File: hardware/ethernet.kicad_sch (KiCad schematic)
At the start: 6 parts, among them U1 TPD4EUSB30, U2 TPD4EUSB30, U3 MagJack-A70-112-331N126

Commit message: Lay out the 4-layer PCB
Route the board on JLCPCB's JLC04161H-7628 stackup (4 layers, 1.6 mm,
ENIG). It fits a 74 mm tube centred on its axis; the tightest part is the
USB-C port J8, 1.8 mm from the wall. DRC gives 0 errors, 0 unconnected
items and a clean schematic parity check. 21 advisory warnings remain on
the 3 mm PoE isolation guide; the README lists them.

Layout:
- the PoE primary side keeps 2.0 mm from everything else on every layer,
  enforced by manafish.kicad_dru, with a primary-only island under U5's
  input half and inner-layer voids next to primary copper
- 100 ohm (Ethernet, CSI) and 90 ohm (USB) pair classes over a solid In1
  ground; GND pours on all layers with stitching vias
- RP2354A core regulator laid out per the RP2350 datasheet, including the
  In1 cut-out under VREG_LX
- fabrication, assembly and isolation-test notes on User.Comments

Schematic and BOM:
- U3 is now the YAGEO JXF0-1012NL 4-pair PoE MagJack, with a new YAGEO
  library and STEP model drawn from datasheet J520
- C21/C24 are 4.7 nF 2 kV KEMET C1812X472KGRACTU (1812)
- U6/U7 are LTV-817S-TA1 (SMD)
- J8's four VBUS pins are joined by a local VBUS label

Libraries:
- Silvertel Ag59800: keep-out on the module-facing layer and the inner
  layer next to it; pads 1-3, 8 and 9 solder-mask defined
- LTC4162 QFN: the exposed-pad paste windows clear the thermal vias
- ABM8-272-T3 courtyard trimmed; 3D model paths fixed for ABM8, SHT45 and
  BMI270

README: new PCB section (stackup, impedance, isolation, assembly,
testing) and the power and Ethernet descriptions brought up to date.
NOTICE: the YAGEO files and the library changes.

Co-Authored-By: Claude Opus 5.5 <noreply@anthropic.com>
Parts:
- U3: value MagJack-A70-112-331N126 -> JXF0-1012NL; footprint CM5IO:TRJG0926HENL -> YAGEO:YAGEO_JXF0-1012NL; symbol CM5IO:MagJack-A70-112-331N126 -> YAGEO:JXF0-1012NL; MPN A70-112-331N126 -> JXF0-1012NL; Manufacturer EDAC -> YAGEO (Pulse); Mouser https://www.mouser.com/ProductDetail/587-A70-112-331N126 -> https://www.mouser.com/ProductDetail/673-JXF0-1012NL; Mouser PN 587-A70-112-331N126 -> 673-JXF0-1012NL
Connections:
- net +3.3V: now also U3.11 (LEDG_A), U3.13 (LEDY_A); no longer U3.15 (LEDY_A), U3.17 (LEDG_A)
- net TRD1_N: now also U3.4 (MD2-); no longer U3.6 (TRD1-)
- net VC1: now also U3.15 (VDC1+); no longer U3.11 (VC1)
- net VC2: now also U3.17 (VDC2+); no longer U3.12 (VC2)
- net VC3: now also U3.18 (VDC2-); no longer U3.13 (VC3)
- net VC4: now also U3.16 (VDC1-); no longer U3.14 (VC4)
- net at R2.1: now also U3.14 (LEDY_K); no longer U3.16 (LEDY_K)
- net at R3.1: now also U3.12 (LEDG_K); no longer U3.18 (LEDG_K)
- net at C1.1, U3.5 (MDCT): now also U3.6 (MDCT); no longer U3.4 (CT)
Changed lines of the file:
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@@
 	)
 	(symbol
-		(lib_id "CM5IO:MagJack-A70-112-331N126")
+		(lib_id "YAGEO:JXF0-1012NL")
 		(at 80.01 106.68 0)
 		(unit 1)
@@
 			)
 		)
-		(property "Value" "MagJack-A70-112-331N126"
+		(property "Value" "JXF0-1012NL"
 			(at 62.23 106.68 0)
 			(show_name no)
@@
 			)
 		)
-		(property "Footprint" "CM5IO:TRJG0926HENL"
+		(property "Footprint" "YAGEO:YAGEO_JXF0-1012NL"
 			(at 80.01 106.68 0)
 			(hide yes)
@@
 			)
 		)
-		(property "Datasheet" "https://www.mouser.com/catalog/specsheets/EDAC_A70-112-331N126.pdf"
+		(property "Datasheet" "https://www.yageogroup.com/content/datasheet/asset/file/DATASHEET_J520"
 			(at 80.01 106.68 0)
 			(hide yes)
@@
 			)
 		)
-		(property "Description" "RJ45 MagJack 1000BASE-T, PoE-capable centre taps, LEDs"
+		(property "Description" "RJ45 MagJack 1000BASE-T, 90 W 4-pair PoE (900 mA per center tap), bi-colour LEDs, THR"
 			(at 80.01 106.68 0)
 			(hide yes)
@@
 			)
 		)
-		(property "Manufacturer" "EDAC"
+		(property "Manufacturer" "YAGEO (Pulse)"
 			(at 80.01 106.68 0)
 			(hide yes)
@@
 			)
 		)
-		(property "MPN" "A70-112-331N126"
+		(property "MPN" "JXF0-1012NL"
 			(at 80.01 106.68 0)
 			(hide yes)
@@
 			)
 		)
-		(property "Mouser PN" "587-A70-112-331N126"
+		(property "Mouser PN" "673-JXF0-1012NL"
 			(at 80.01 106.68 0)
 			(hide yes)
@@
 			)
 		)
-		(property "Mouser" "https://www.mouser.com/ProductDetail/587-A70-112-331N126"
+		(property "Mouser" "https://www.mouser.com/ProductDetail/673-JXF0-1012NL"
 			(at 80.01 106.68 0)
 			(hide yes)

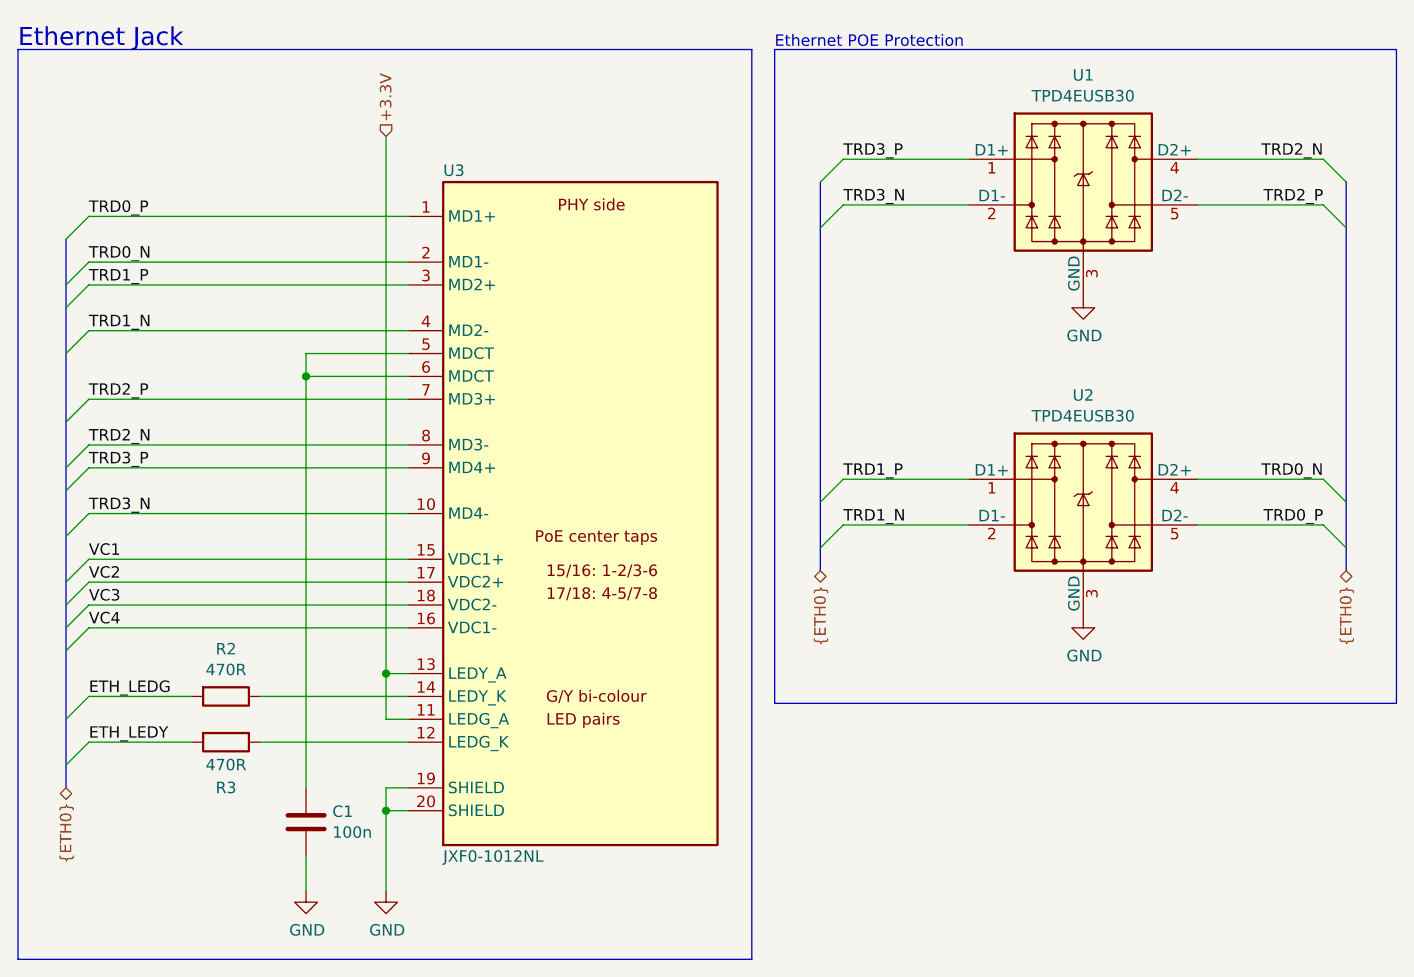
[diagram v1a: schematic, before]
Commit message: Add second camera, magnet load switch and schematic fixes
- Second camera J11 on MIPI1: I2C on ID_SD/ID_SC with 2.2k pull-ups,
  power enable on GPIO14/15 (CAM1_GPIO0/1); both cameras take 3.3 V
  from CM5_3.3V
- Magnet power switch: IC9 output is now +5V_AON, TPS22965 load switch
  IC15 drives +5V, J12 carries +5V_AON / MAG_ON / GND with R29
  pull-down; new TPS22965 symbol library
- Power: 4 A TPSM53604, 8 mOhm input sense resistor, C39/C40 bulk caps,
  F1-F3 battery polyfuses; 5 V raised to 5.115 V (R24 2.43k, 0.5 %
  feedback resistors); 47 uF at the CM5 5 V pins
- BMI270 on SPI and WSEN-PADS on I2C in serial_peripherals.kicad_sch
- Breakout headers J9/J13 with 5 V, 3.3 V and GND
- References renamed U -> IC; net classes for DPHY1, +5V, +5V_AON, +3.3V
- ERC clean (0 errors, 0 warnings); PCB update from the schematic is
  still in progress

Co-Authored-By: Claude Opus 5.5 <noreply@anthropic.com>
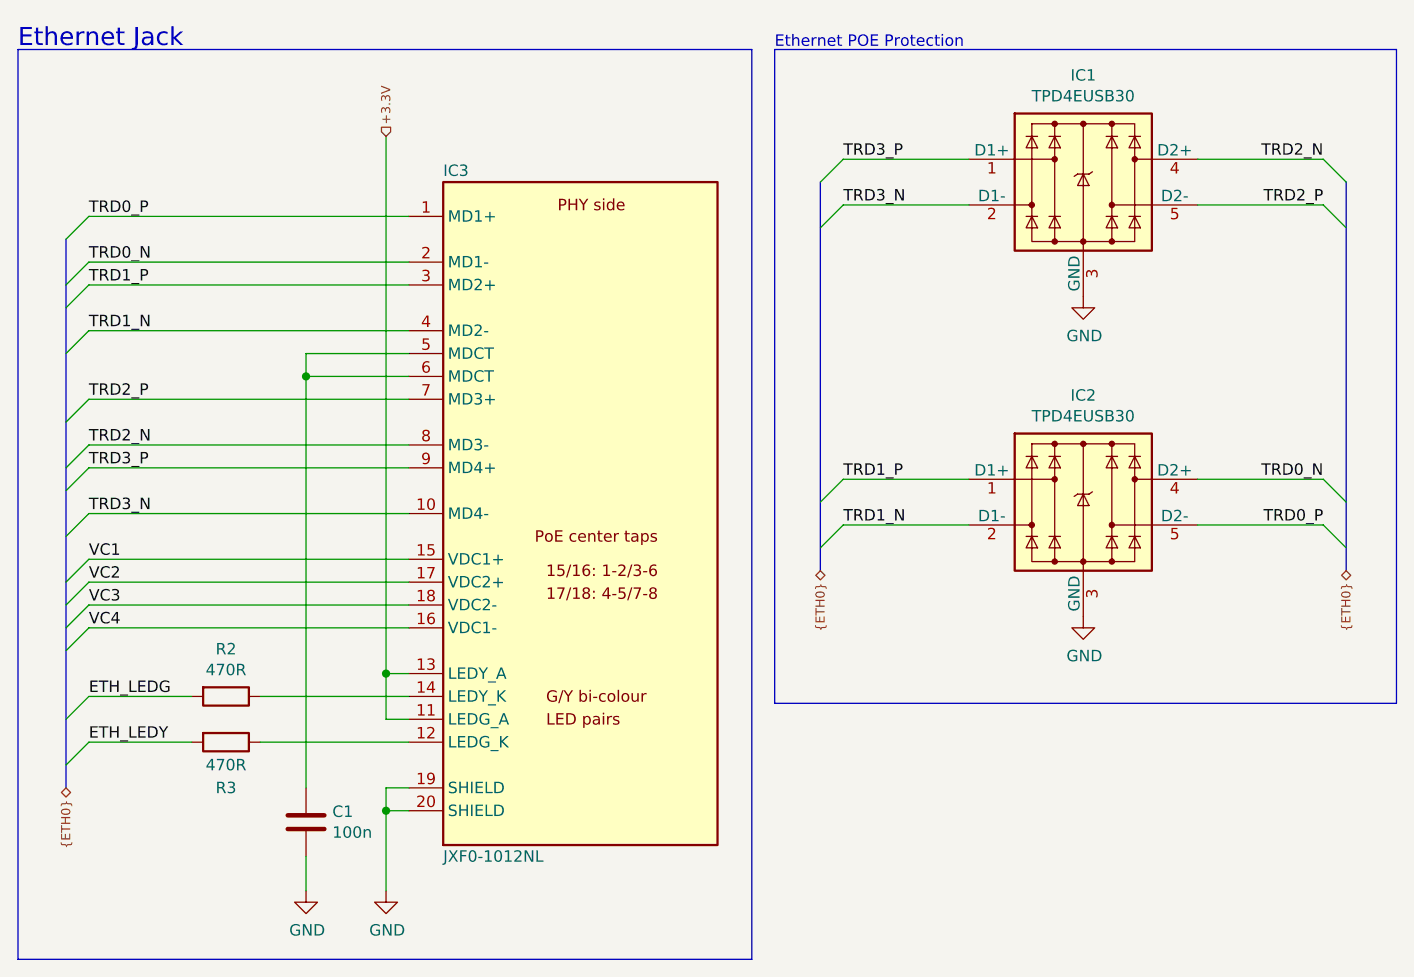
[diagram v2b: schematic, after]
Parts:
- renumbered U1 to IC1, U2 to IC2, U3 to IC3
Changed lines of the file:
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@@
 		(effects
 			(font
-				(size 1.27 1.27)
+				(size 1.016 1.016)
 			)
 			(justify right)
@@
 		(effects
 			(font
-				(size 1.27 1.27)
+				(size 1.016 1.016)
 			)
 			(justify left)
@@
 		(effects
 			(font
-				(size 1.27 1.27)
+				(size 1.016 1.016)
 			)
 			(justify right)
@@
 		(effects
 			(font
-				(size 1.27 1.27)
+				(size 1.016 1.016)
 			)
 			(justify right)
@@
 		(in_pos_files yes)
 		(dnp no)
-		(property "Reference" "U3"
+		(property "Reference" "IC3"
 			(at 62.23 30.48 0)
 			(show_name no)
@@
 			(project "manafish"
 				(path "/37283e3e-a087-4659-9b29-171eab26a1f6/ba09456f-d29b-4907-909f-45263bd46633"
-					(reference "U3")
+					(reference "IC3")
 					(unit 1)
 				)
@@
 		(in_pos_files yes)
 		(dnp no)
-		(property "Reference" "U1"
+		(property "Reference" "IC1"
 			(at 133.35 19.8882 0)
 			(show_name no)
@@
 			(project "manafish"
 				(path "/37283e3e-a087-4659-9b29-171eab26a1f6/ba09456f-d29b-4907-909f-45263bd46633"
-					(reference "U1")
+					(reference "IC1")
 					(unit 1)
 				)
@@
 		(in_pos_files yes)
 		(dnp no)
-		(property "Reference" "U2"
+		(property "Reference" "IC2"
 			(at 133.35 55.4482 0)
 			(show_name no)
@@
 			(project "manafish"
 				(path "/37283e3e-a087-4659-9b29-171eab26a1f6/ba09456f-d29b-4907-909f-45263bd46633"
-					(reference "U2")
+					(reference "IC2")
 					(unit 1)
 				)

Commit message: Add LCSC part numbers and links, fix J7 part number
- Every part found on LCSC gets an "LCSC PN" (C-number) and an "LCSC" product
  link field, in the schematic and on the PCB footprints. Exact matches where
  LCSC lists the part; equivalents with the same specs where it does not or
  has no stock (C46, C26/C28/C30/C33/C34/C40, C29, C31, R6/R7, R21, R24,
  J3/J4, J7/J9/J13). Left empty: IC3, IC5 (not on LCSC), IC10, IC12
  (JLCPCB-only listings).
- J7: the MPN 61301421121 is a 2.54 mm header, but the footprint is 1.27 mm.
  Now Wurth 62201421121 (WR-PHD 1.27 mm 2x7) with matching description,
  datasheet and Mouser fields.
- Interactive HTML BOM in hardware/bom; KiCad project file re-saved.

Co-Authored-By: Claude Opus 5.5 <noreply@anthropic.com>
Claude-Session: https://claude.ai/code/session_01AhLYztcZikG9g81njGtEr1
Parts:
- C1: LCSC (none) -> https://www.lcsc.com/product-detail/C71629.html; LCSC PN (none) -> C71629
- IC1, IC2: LCSC (none) -> https://www.lcsc.com/product-detail/C90627.html; LCSC PN (none) -> C90627
- R2, R3: LCSC (none) -> https://www.lcsc.com/product-detail/C114877.html; LCSC PN (none) -> C114877
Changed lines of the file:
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@@
+			)
+		)
+		(property "LCSC PN" "C114877"
+			(at 38.1 93.98 0)
+			(hide yes)
+			(show_name no)
+			(do_not_autoplace no)
+			(effects
+				(font
+					(size 1.27 1.27)
+				)
+			)
+		)
+		(property "LCSC" "https://www.lcsc.com/product-detail/C114877.html"
+			(at 38.1 93.98 0)
+			(hide yes)
+			(show_name no)
+			(do_not_autoplace no)
+			(effects
+				(font
+					(size 1.27 1.27)
+				)
 			)
 		)
@@
 			)
 		)
+		(property "LCSC PN" "C114877"
+			(at 38.1 88.9 0)
+			(hide yes)
+			(show_name no)
+			(do_not_autoplace no)
+			(effects
+				(font
+					(size 1.27 1.27)
+				)
+			)
+		)
+		(property "LCSC" "https://www.lcsc.com/product-detail/C114877.html"
+			(at 38.1 88.9 0)
+			(hide yes)
+			(show_name no)
+			(do_not_autoplace no)
+			(effects
+				(font
+					(size 1.27 1.27)
+				)
+			)
+		)
 		(pin "1"
 		)
@@
 			)
 		)
+		(property "LCSC PN" "C90627"
+			(at 133.35 31.75 0)
+			(hide yes)
+			(show_name no)
+			(do_not_autoplace no)
+			(effects
+				(font
+					(size 1.27 1.27)
+				)
+			)
+		)
+		(property "LCSC" "https://www.lcsc.com/product-detail/C90627.html"
+			(at 133.35 31.75 0)
+			(hide yes)
+			(show_name no)
+			(do_not_autoplace no)
+			(effects
+				(font
+					(size 1.27 1.27)
+				)
+			)
+		)
 		(pin "1"
 		)
@@
 			)
 		)
+		(property "LCSC PN" "C71629"
+			(at 46.99 102.87 0)
+			(hide yes)
+			(show_name no)
+			(do_not_autoplace no)
+			(effects
+				(font
+					(size 1.27 1.27)
+				)
+			)
+		)
+		(property "LCSC" "https://www.lcsc.com/product-detail/C71629.html"
+			(at 46.99 102.87 0)
+			(hide yes)
+			(show_name no)
+			(do_not_autoplace no)
+			(effects
+				(font
+					(size 1.27 1.27)
+				)
+			)
+		)
 		(pin "1"
 		)
@@
 			(at 133.35 67.31 0)
 			(hide yes)
+			(show_name no)
+			(do_not_autoplace no)
+			(effects
+				(font
+					(size 1.27 1.27)
+				)
+			)
+		)
+		(property "LCSC PN" "C90627"
+			(at 133.35 67.31 0)
+			(hide yes)
+			(show_name no)
+			(do_not_autoplace no)
+			(effects
+				(font
+					(size 1.27 1.27)
+				)
+			)
+		)
+		(property "LCSC" "https://www.lcsc.com/product-detail/C90627.html"
+			(at 133.35 67.31 0)
+			(hide yes)
